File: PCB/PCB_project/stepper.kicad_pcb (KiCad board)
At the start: 2 copper layers, 65 x 105 mm, 9 parts, among them J1 DB15_Female_HighDensity, J2 DB15_Female_HighDensity, J3 DB15_Female_HighDensity, U1 NUCLEO-L432KC, U2 AMIS-30543-POLOLU, U3 AMIS-30543-POLOLU, U4 AMIS-30543-POLOLU, U5 +12V, U6 GND

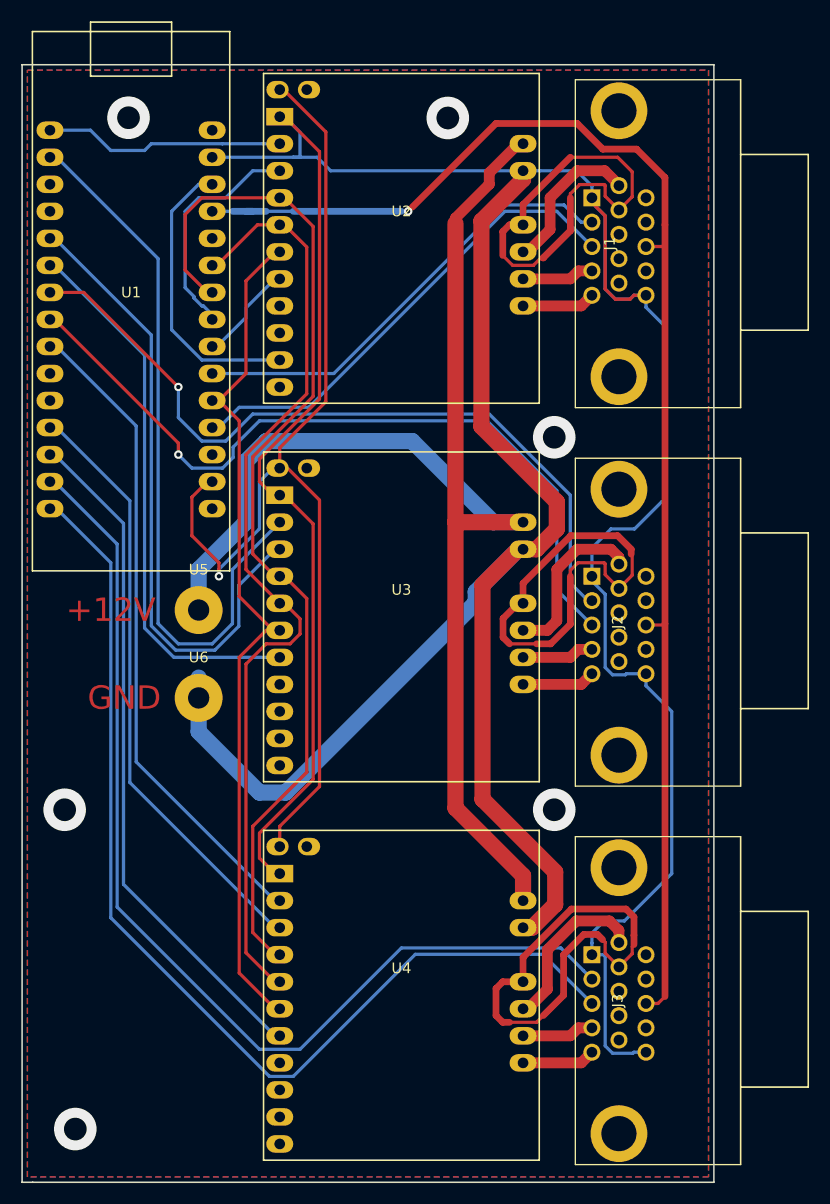
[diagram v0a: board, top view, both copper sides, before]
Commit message: PCP updated after pin swap
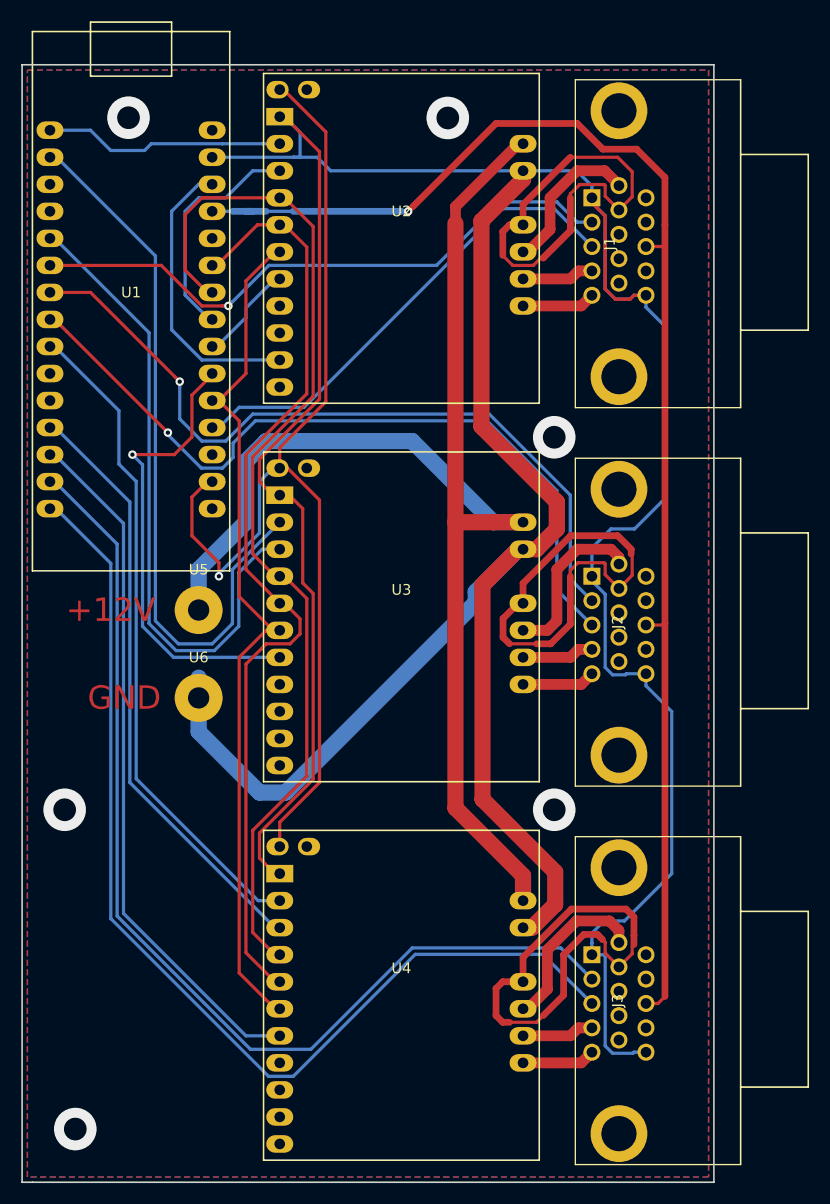
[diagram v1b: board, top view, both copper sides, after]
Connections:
- J1 pad 2: FLIMIT1 -> FLIMIT3
- J1 pad 3: RLIMIT1 -> RLIMIT3
- J3 pad 2: FLIMIT3 -> FLIMIT1
- J3 pad 3: RLIMIT3 -> RLIMIT1
- U1 pad 1: NXT1 -> NXT3
- U1 pad 12: DIR3 -> DIR1
- U1 pad 13: CS3 -> CS1
- U1 pad 14: FLIMIT3 -> FLIMIT1
- U1 pad 15: RLIMIT3 -> RLIMIT1
- U1 pad 23: DIR1 -> DIR3
- U1 pad 24: CS1 -> CS3
- U1 pad 25: FLIMIT1 -> CS2
- U1 pad 27: RLIMIT1 -> RLIMIT3
- U1 pad 6: CS2 -> FLIMIT3
- U1 pad 9: NXT3 -> NXT1
- U2 pad 4: NXT1 -> NXT3
- U2 pad 5: DIR1 -> DIR3
- U2 pad 9: CS1 -> CS3
- U4 pad 4: NXT3 -> NXT1
- U4 pad 5: DIR3 -> DIR1
- U4 pad 9: CS3 -> CS1
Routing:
- net CS1: track 9.50 -> 65.7 mm
- net FLIMIT1: track 42.9 -> 98.6 mm
- net CS3: track 64.1 -> 9.50 mm
- net RLIMIT1: track 45.5 -> 99.2 mm
- net RLIMIT3: track 99.2 -> 45.7 mm
- net FLIMIT3: track 98.1 -> 57.8 mm, vias 0 -> 1
- net NXT1: track 23.1 -> 62.5 mm
- net NXT3: track 61.6 -> 23.1 mm
- net DIR3: track 56.6 -> 21.8 mm
- net DIR1: track 22.4 -> 56.5 mm
- net CS2: track 51.9 -> 43.7 mm, vias 0 -> 1
- net DIR2: track 59.8 -> 60.5 mm

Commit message: Adaptatations in pinout for future switch panel
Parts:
- added U7: EIN, TestPoint:TestPoint_Plated_Hole_D2.0mm, F.Cu at (141.5, 98.8)
- added U8: +3V3, TestPoint:TestPoint_Plated_Hole_D2.0mm, F.Cu at (141.5, 103.5)
- added U9: GND, TestPoint:TestPoint_Plated_Hole_D2.0mm, F.Cu at (141.5, 108.1)
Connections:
- U1 pad 25: CS2 -> EIN
- U1 pad 30: Net-(U1-Pad30) -> CS2
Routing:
- net EIN: track 0.00 -> 32.5 mm
- net +3V3: track 102.3 -> 120.2 mm
- net Net-(J1-Pad7): track 47.7 -> 60.4 mm
- net CS2: track 43.7 -> 40.2 mm
- net FLIMIT2: track 71.7 -> 70.3 mm
- net Net-(J3-Pad7): track 47.5 -> 46.6 mm
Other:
- board text added: "12V"
- board text added: "3V3"
- board text added: "GPIO"
- board text added: "Kacper Oreszczuk"
- board text added: "MAY 2020"
- board text removed: "+12V"
